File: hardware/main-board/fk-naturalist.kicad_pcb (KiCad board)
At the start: 2 copper layers, 103 x 37.5 mm, 128 parts, among them J1 RF-SMA-EDGE, J10 S2B-PH-SM4-TB, J11 RF-SMA-EDGE, J12 CONN_01x02, J13 CONN_01x06, J14 CONN_01x02, J2 CONN_01x02, J3 S2B-PH-SM4-TB, J4 Conn_01x01, J5 CONN_01x03_SERIAL, J6 CONN_01x09, J7 CONN_02x05_SWD, J8 CONN_01x02, J9 MICRO-USB, M10 FIDUCIAL, M11 FIDUCIAL, M2 FIDUCIAL, M5 FIDUCIAL, M7 MICRO-SD, M8 FIDUCIAL, M9 FIDUCIAL, Q1 2N7002LT1G, SW1 SPNO, SW2 SPNO, U1 ATWINC1500-MR210PA, U10 FGPMMOPA6H, U11 MAX1704XX, U12 TPS2052B, U13 SK6812, U14 MCP1700T-3302E/MB, U2 ATSAMD21G18A-AU, U3 RFM95W, U4 24AA02E64, U5 S25FL116K0XMFI041, U6 BQ24074RGTT, U7 PCF8523, U8 TL5209, U9 TL5209, Y1 FC-135, Y2 FC-135

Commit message: Plot and bump version.
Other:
- board text added: "v0.11"
- board text removed: "v0.10"
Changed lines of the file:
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@@
   )
   (setup
-    (last_trace_width 0.381)
+    (last_trace_width 0.254)
     (user_trace_width 0.2032)
     (user_trace_width 0.254)
@@
     (effects (font (size 1 1) (thickness 0.2)))
   )
-  (gr_text v0.10 (at 79.756 110.0963 180) (layer F.SilkS)
+  (gr_text v0.11 (at 79.756 110.0963 180) (layer F.SilkS)
     (effects (font (size 1 1) (thickness 0.2)))
   )
@@
   (segment (start 122.294522 143.440022) (end 122.936 144.0815) (width 0.381) (layer F.Cu) (net 109))
   (via (at 122.936 144.0815) (size 0.5) (drill 0.3) (layers F.Cu B.Cu) (net 109))
-  (segment (start 152.7175 129.94132) (end 152.76322 129.8956) (width 0.254) (layer B.Cu) (net 134))
   (via (at 148.463 142.3035) (size 0.5) (drill 0.3) (layers F.Cu B.Cu) (net 109))
   (segment (start 120.725006 145.288) (end 120.3071 145.288) (width 0.381) (layer B.Cu) (net 109))
@@
   (segment (start 119.5705 140.147) (end 119.5705 142.937324) (width 0.381) (layer F.Cu) (net 109))
   (segment (start 119.5705 142.937324) (end 120.073198 143.440022) (width 0.381) (layer F.Cu) (net 109))
-  (segment (start 152.6794 129.81178) (end 152.76322 129.8956) (width 0.254) (layer B.Cu) (net 134))
-  (segment (start 152.76322 129.39649) (end 152.76322 129.8956) (width 0.254) (layer B.Cu) (net 134))
-  (segment (start 144.676353 126.9619) (end 150.32863 126.9619) (width 0.254) (layer B.Cu) (net 134))
-  (segment (start 144.1664 126.9619) (end 144.0815 127.0468) (width 0.254) (layer B.Cu) (net 134))
-  (via (at 144.0815 127.0468) (size 0.5) (drill 0.3) (layers F.Cu B.Cu) (net 134))
-  (segment (start 144.676353 126.9619) (end 144.1664 126.9619) (width 0.254) (layer B.Cu) (net 134))
-  (segment (start 144.0815 129.5344) (end 144.0829 129.5358) (width 0.254) (layer F.Cu) (net 134))
-  (segment (start 144.0815 127.0468) (end 144.0815 129.5344) (width 0.254) (layer F.Cu) (net 134))
   (segment (start 122.936 144.0815) (end 127.3937 144.0815) (width 0.381) (layer B.Cu) (net 109))
   (segment (start 129.1717 142.3035) (end 127.3937 144.0815) (width 0.381) (layer B.Cu) (net 109))
@@
   (segment (start 148.844 132.2959) (end 149.706699 131.433201) (width 0.381) (layer F.Cu) (net 109))
   (segment (start 148.712999 132.426901) (end 148.844 132.2959) (width 0.381) (layer F.Cu) (net 109))
-  (via (at 152.7683 128.1049) (size 0.5) (drill 0.3) (layers F.Cu B.Cu) (net 134))
-  (segment (start 152.781 128.0922) (end 152.7683 128.1049) (width 0.381) (layer F.Cu) (net 134))
-  (segment (start 154.4456 128.0922) (end 152.781 128.0922) (width 0.381) (layer F.Cu) (net 134))
-  (segment (start 152.7683 129.89052) (end 152.76322 129.8956) (width 0.381) (layer B.Cu) (net 134))
-  (segment (start 152.7683 128.1049) (end 152.7683 129.89052) (width 0.381) (layer B.Cu) (net 134))
-  (segment (start 154.4456 128.0922) (end 154.4456 129.7559) (width 0.254) (layer F.Cu) (net 134))
-  (segment (start 154.431501 129.769999) (end 154.4456 129.7559) (width 0.254) (layer F.Cu) (net 134))
-  (segment (start 151.47163 128.1049) (end 150.32863 126.9619) (width 0.254) (layer B.Cu) (net 134))
-  (segment (start 152.7683 128.1049) (end 151.47163 128.1049) (width 0.254) (layer B.Cu) (net 134))
   (segment (start 117.0305 140.147) (end 117.0305 141.401) (width 0.254) (layer F.Cu) (net 110))
   (segment (start 117.0305 141.401) (end 116.255 142.1765) (width 0.254) (layer F.Cu) (net 110))
@@
   (segment (start 112.9157 117.0559) (end 114.5213 115.4503) (width 0.254) (layer F.Cu) (net 133))
   (segment (start 112.9157 122.4534) (end 112.9157 117.0559) (width 0.254) (layer F.Cu) (net 133))
+  (segment (start 152.7175 129.94132) (end 152.76322 129.8956) (width 0.254) (layer B.Cu) (net 134))
+  (segment (start 152.6794 129.81178) (end 152.76322 129.8956) (width 0.254) (layer B.Cu) (net 134))
+  (segment (start 152.76322 129.39649) (end 152.76322 129.8956) (width 0.254) (layer B.Cu) (net 134))
+  (segment (start 144.676353 126.9619) (end 150.32863 126.9619) (width 0.254) (layer B.Cu) (net 134))
+  (segment (start 144.1664 126.9619) (end 144.0815 127.0468) (width 0.254) (layer B.Cu) (net 134))
+  (via (at 144.0815 127.0468) (size 0.5) (drill 0.3) (layers F.Cu B.Cu) (net 134))
+  (segment (start 144.676353 126.9619) (end 144.1664 126.9619) (width 0.254) (layer B.Cu) (net 134))
+  (segment (start 144.0815 129.5344) (end 144.0829 129.5358) (width 0.254) (layer F.Cu) (net 134))
+  (segment (start 144.0815 127.0468) (end 144.0815 129.5344) (width 0.254) (layer F.Cu) (net 134))
+  (via (at 152.7683 128.1049) (size 0.5) (drill 0.3) (layers F.Cu B.Cu) (net 134))
+  (segment (start 152.781 128.0922) (end 152.7683 128.1049) (width 0.381) (layer F.Cu) (net 134))
+  (segment (start 154.4456 128.0922) (end 152.781 128.0922) (width 0.381) (layer F.Cu) (net 134))
+  (segment (start 152.7683 129.89052) (end 152.76322 129.8956) (width 0.381) (layer B.Cu) (net 134))
+  (segment (start 152.7683 128.1049) (end 152.7683 129.89052) (width 0.381) (layer B.Cu) (net 134))
+  (segment (start 154.4456 128.0922) (end 154.4456 129.7559) (width 0.254) (layer F.Cu) (net 134))
+  (segment (start 154.431501 129.769999) (end 154.4456 129.7559) (width 0.254) (layer F.Cu) (net 134))
+  (segment (start 151.47163 128.1049) (end 150.32863 126.9619) (width 0.254) (layer B.Cu) (net 134))
+  (segment (start 152.7683 128.1049) (end 151.47163 128.1049) (width 0.254) (layer B.Cu) (net 134))
   (segment (start 154.419702 131.445) (end 154.431501 131.433201) (width 0.254) (layer F.Cu) (net 134))
   (segment (start 152.5388 131.445) (end 154.419702 131.445) (width 0.254) (layer F.Cu) (net 134))

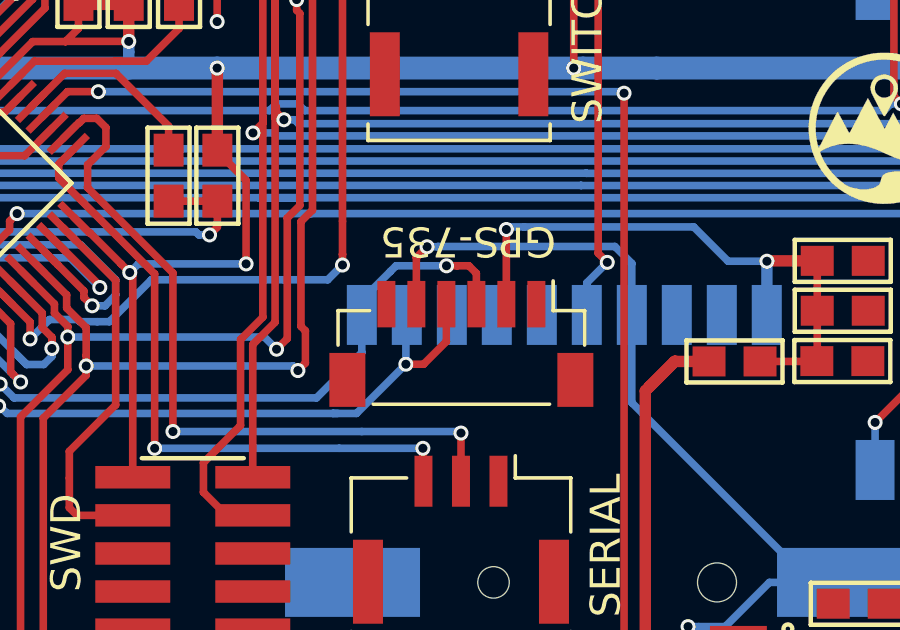
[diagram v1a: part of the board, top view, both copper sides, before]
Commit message: Fix Rx/Tx on backup GPS.
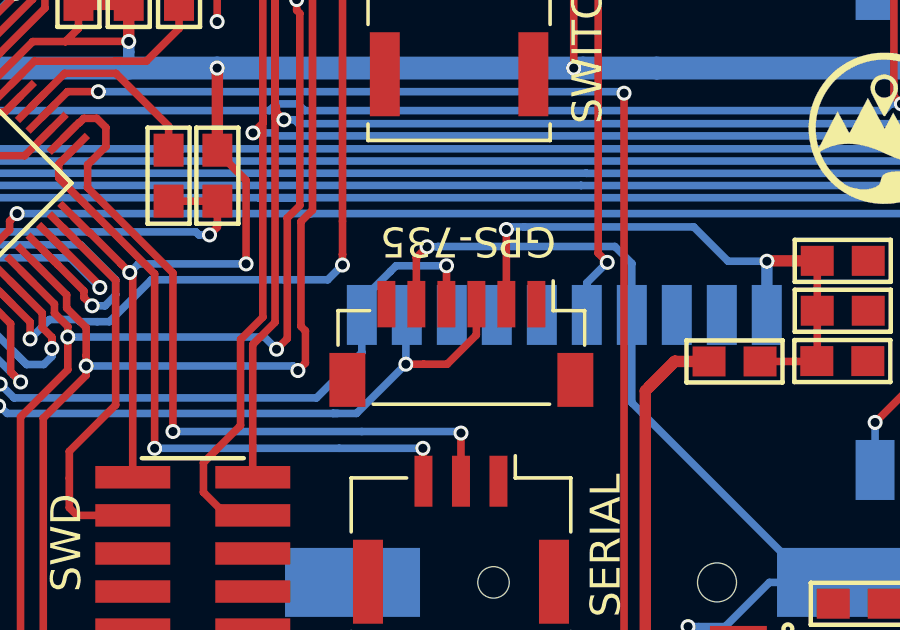
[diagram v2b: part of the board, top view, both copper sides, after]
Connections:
- J13 pad 3: /GPS_RX -> /GPS_TX
- J13 pad 4: /GPS_TX -> /GPS_RX
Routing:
- net /GPS_TX: track 22.1 -> 23.0 mm
- net /GPS_RX: track 22.7 -> 21.9 mm
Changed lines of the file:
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@@
     (thickness 1.6)
     (drawings 28)
-    (tracks 1616)
+    (tracks 1614)
     (zones 0)
     (modules 128)
@@
       (net 134 "Net-(C31-Pad2)"))
     (pad 3 smd rect (at -0.5 1.325 180) (size 0.6 1.55) (layers F.Cu F.Paste F.Mask)
-      (net 90 /GPS_RX))
-    (pad 4 smd rect (at 0.5 1.325 180) (size 0.6 1.55) (layers F.Cu F.Paste F.Mask)
       (net 89 /GPS_TX))
+    (pad 4 smd rect (at 0.5 1.325 180) (size 0.6 1.55) (layers F.Cu F.Paste F.Mask)
+      (net 90 /GPS_RX))
     (pad 5 smd rect (at 1.5 1.325 180) (size 0.6 1.55) (layers F.Cu F.Paste F.Mask)
       (net 25 /BAT_BACKUP))
@@
   (segment (start 140.733085 129.926775) (end 140.76426 129.8956) (width 0.254) (layer B.Cu) (net 89))
   (segment (start 140.733085 131.53767) (end 140.733085 129.926775) (width 0.254) (layer B.Cu) (net 89))
-  (segment (start 142.0876 129.5311) (end 142.0829 129.5358) (width 0.254) (layer F.Cu) (net 89))
-  (segment (start 141.3256 131.53767) (end 142.0829 130.78037) (width 0.254) (layer F.Cu) (net 89))
+  (segment (start 142.0876 129.5311) (end 142.0829 129.5358) (width 0.254) (layer F.Cu) (net 90))
   (segment (start 140.733085 131.53767) (end 141.3256 131.53767) (width 0.254) (layer F.Cu) (net 89))
-  (segment (start 142.0829 130.78037) (end 142.0829 129.5358) (width 0.254) (layer F.Cu) (net 89))
+  (segment (start 142.11003 131.53767) (end 141.3256 131.53767) (width 0.254) (layer F.Cu) (net 89))
+  (segment (start 143.0829 130.5648) (end 142.11003 131.53767) (width 0.254) (layer F.Cu) (net 89))
+  (segment (start 143.0829 129.5358) (end 143.0829 130.5648) (width 0.254) (layer F.Cu) (net 89))
   (segment (start 139.26566 129.8956) (end 139.26566 131.14909) (width 0.254) (layer B.Cu) (net 90))
   (segment (start 139.26566 131.14909) (end 137.754796 132.659954) (width 0.254) (layer B.Cu) (net 90))
@@
   (segment (start 127.006607 130.34508) (end 127.006607 131.994436) (width 0.254) (layer F.Cu) (net 90))
   (segment (start 126.476278 129.814751) (end 127.006607 130.34508) (width 0.254) (layer F.Cu) (net 90))
-  (segment (start 142.441153 128.2573) (end 142.0876 128.2573) (width 0.254) (layer F.Cu) (net 90))
-  (segment (start 142.8334 128.2573) (end 142.441153 128.2573) (width 0.254) (layer F.Cu) (net 90))
-  (segment (start 143.0829 128.5068) (end 142.8334 128.2573) (width 0.254) (layer F.Cu) (net 90))
-  (segment (start 143.0829 129.5358) (end 143.0829 128.5068) (width 0.254) (layer F.Cu) (net 90))
+  (segment (start 142.0876 128.2573) (end 142.0876 129.5311) (width 0.254) (layer F.Cu) (net 90))
   (segment (start 170.3728 135.0635) (end 170.3728 133.5278) (width 1.27) (layer B.Cu) (net 91))
   (segment (start 170.3728 133.5278) (end 170.3728 132.7935) (width 1.27) (layer B.Cu) (net 91))

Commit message: Naturalist module enable pin is A5, D9 is used for I2S.
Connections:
- U2 pad 47: /D9_MODULE_EN -> /A5_MODULE_EN
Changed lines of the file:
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@@
     (zones 0)
     (modules 128)
-    (nets 135)
+    (nets 136)
   )
   (page A4)
@@
   (net 133 /I2S_DATA)
   (net 134 "Net-(C31-Pad2)")
+  (net 135 /A5_MODULE_EN)
   (net_class Default "This is the default net class."
     (clearance 0.1524)
@@
     (add_net /A3)
     (add_net /A4_GPS_EN)
+    (add_net /A5_MODULE_EN)
     (add_net /BAT_BACKUP)
     (add_net /CHG)
@@
       (effects (font (size 1 1) (thickness 0.15)))
     )
-    (fp_text value 2N7002LT1G (at 3.0734 -0.1308) (layer F.Fab)
+    (fp_text value 2N7002LT1G (at 3.0734 -0.1308) (layer F.Fab) hide
       (effects (font (size 1 1) (thickness 0.15)))
     )
@@
       (net 126 /D1_RADIO_D1))
     (pad 47 smd rect (at -2.25 -4.35 45) (size 1.3 0.25) (layers F.Cu F.Paste F.Mask)
-      (net 125 /D9_MODULE_EN))
+      (net 135 /A5_MODULE_EN))
     (pad 48 smd rect (at -2.75 -4.35 45) (size 1.3 0.25) (layers F.Cu F.Paste F.Mask)
       (net 96 /PERIPH_EN))
@@
       (effects (font (size 1 1) (thickness 0.15)))
     )
-    (fp_text value CONN_01x09 (at 0 4 180) (layer F.Fab)
+    (fp_text value CONN_01x09 (at 0 4 180) (layer F.Fab) hide
       (effects (font (size 1 1) (thickness 0.15)))
     )
@@
   (segment (start 140.733085 129.926775) (end 140.76426 129.8956) (width 0.254) (layer B.Cu) (net 89))
   (segment (start 140.733085 131.53767) (end 140.733085 129.926775) (width 0.254) (layer B.Cu) (net 89))
-  (segment (start 142.0876 129.5311) (end 142.0829 129.5358) (width 0.254) (layer F.Cu) (net 90))
   (segment (start 140.733085 131.53767) (end 141.3256 131.53767) (width 0.254) (layer F.Cu) (net 89))
   (segment (start 142.11003 131.53767) (end 141.3256 131.53767) (width 0.254) (layer F.Cu) (net 89))
   (segment (start 143.0829 130.5648) (end 142.11003 131.53767) (width 0.254) (layer F.Cu) (net 89))
   (segment (start 143.0829 129.5358) (end 143.0829 130.5648) (width 0.254) (layer F.Cu) (net 89))
+  (segment (start 142.0876 129.5311) (end 142.0829 129.5358) (width 0.254) (layer F.Cu) (net 90))
   (segment (start 139.26566 129.8956) (end 139.26566 131.14909) (width 0.254) (layer B.Cu) (net 90))
   (segment (start 139.26566 131.14909) (end 137.754796 132.659954) (width 0.254) (layer B.Cu) (net 90))
